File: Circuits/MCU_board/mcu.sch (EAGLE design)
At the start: 72 parts, among them IC1 RP111N331B-TR-FE, IC2 FT230XS, U1 TCA9548APWR, U2 USBLC6-2P6, U4 LSM9DS1, U5 STM32L452RECT6

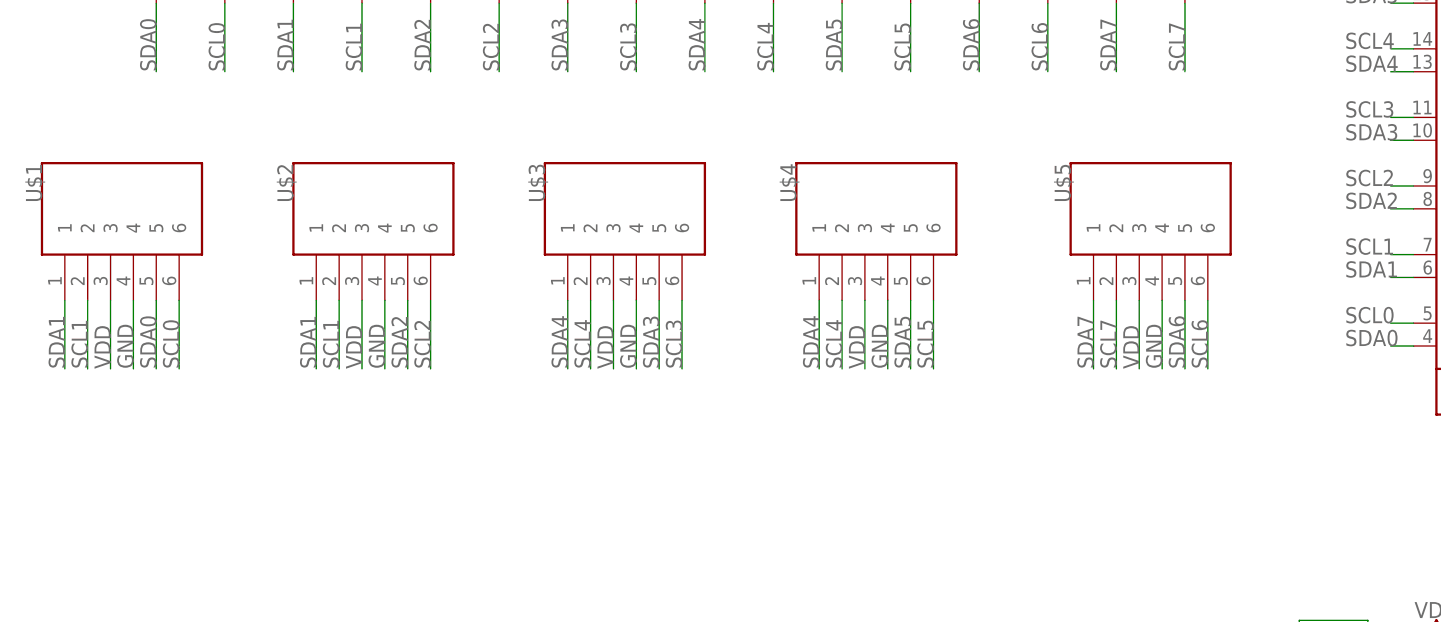
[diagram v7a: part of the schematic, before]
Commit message: Moved connectors to top layer, fixed connector signals
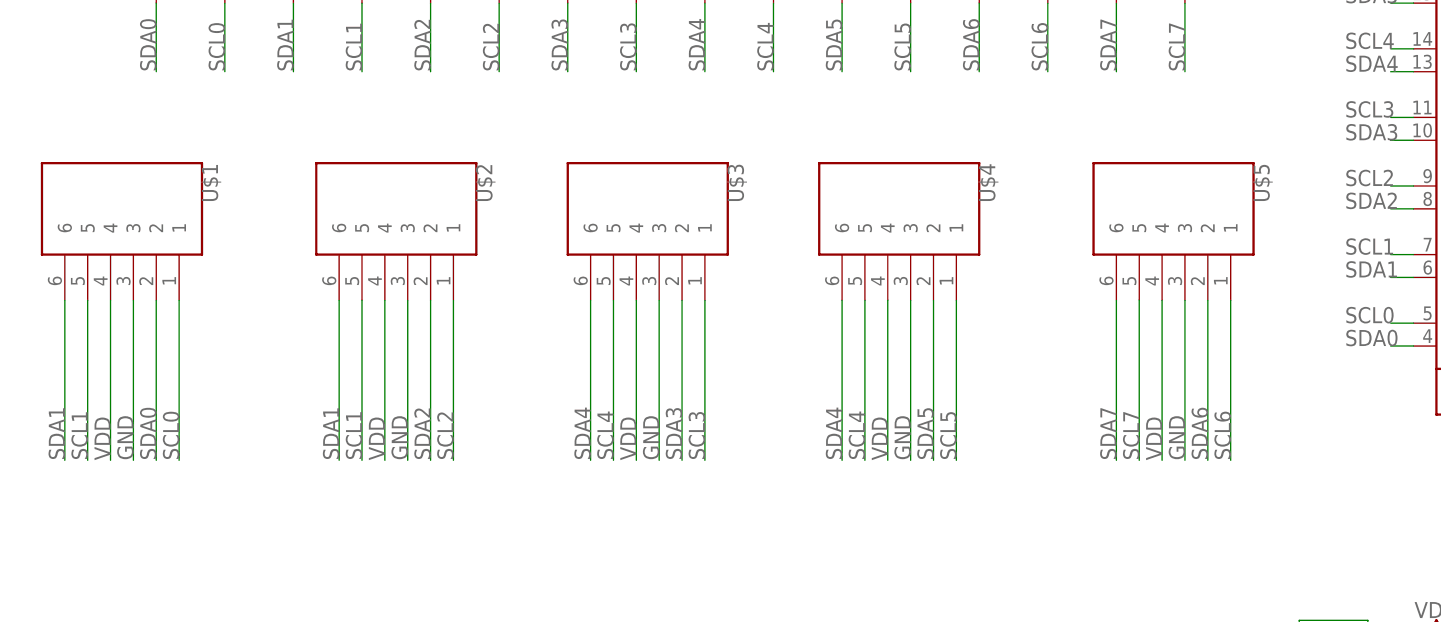
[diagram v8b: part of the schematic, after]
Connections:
- net GND: now also U$1.3, U$2.3, U$3.3, U$4.3, U$5.3; no longer U$1.4, U$2.4, U$3.4, U$4.4, U$5.4
- net SCL0: now also U$1.1; no longer U$1.6
- net SCL1: now also U$1.5, U$2.5; no longer U$1.2, U$2.2
- net SCL2: now also U$2.1; no longer U$2.6
- net SCL3: now also U$3.1; no longer U$3.6
- net SCL4: now also U$3.5, U$4.5; no longer U$3.2, U$4.2
- net SCL5: now also U$4.1; no longer U$4.6
- net SCL6: now also U$5.1; no longer U$5.6
- net SCL7: now also U$5.5; no longer U$5.2
- net SDA0: now also U$1.2; no longer U$1.5
- net SDA1: now also U$1.6, U$2.6; no longer U$1.1, U$2.1
- net SDA2: now also U$2.2; no longer U$2.5
- net SDA3: now also U$3.2; no longer U$3.5
- net SDA4: now also U$3.6, U$4.6; no longer U$3.1, U$4.1
- net SDA5: now also U$4.2; no longer U$4.5
- net SDA6: now also U$5.2; no longer U$5.5
- net SDA7: now also U$5.6; no longer U$5.1
- net VDD: now also U$1.4, U$2.4, U$3.4, U$4.4, U$5.4; no longer U$1.3, U$2.3, U$3.3, U$4.3, U$5.3
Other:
- moved on the sheet: U$2, U$3, U$4, U$5
